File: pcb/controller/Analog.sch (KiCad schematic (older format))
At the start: 0 parts

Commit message: controller schematic capture almost done
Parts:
- added C? (x16): 0.47u, symbol Device:C
- added C? (x5): C, symbol Device:C
- added C? (x6): 4.7u, symbol Device:C
- added D? (x2): D, symbol Device:D
- added FB? (x2): Ferrite_Bead, symbol Device:Ferrite_Bead
- added J? (x2): Conn_Coaxial, symbol Connector:Conn_Coaxial
- added R? (x17): R, symbol Device:R
- added R?: 51, symbol Device:R
- added U?: TLV3501AIDBVR, symbol wbraun_ic_lib:TLV3501AIDBVR
- added U?: MCP6561-OT, Package_TO_SOT_SMD:SOT-23-5, symbol Amplifier_Operational:MCP6561-OT
- added U?: AD9609, symbol wbraun_ic_lib:AD9609
- added U?: THS4551RGT, symbol wbraun_ic_lib:THS4551RGT
- added U?: SG3225, symbol wbraun_ic_lib:SG3225
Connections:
- new net: C?.1, R?.1, R?.2, U?.1 (-)
- new net: C?.2, R?.2, U?.3 (+)
- new net: R?.1, R?.2, R?.2, U?.3 (+)
- new net: R?.1, R?.2, U?.4 (-)
- new net: C?.2, U?.1 (CLK+)
- new net: C?.2, U?.2 (CLK-)
- new net: C?.2, D?.1 (K), D?.2 (A), J?.1 (In)
- new net: C?.2, J?.1 (In), R?.2
- new net: C?.1, R?.1, U?.1 (FB-)
- new net: C?.2, R?.1, U?.2 (IN+)
- new net: C?.2, R?.1, U?.3 (IN-)
- new net: C?.1, R?.1, U?.4 (FB+)
- new net: C?.1, R?.1, R?.2, R?.2
- new net: C?.1, R?.2 (x3)
- new net: C?.2, R?.1, R?.2, R?.2
- new net +1V8: C?.2, C?.2, C?.2, C?.2, C?.2, U?.24 (AVDD), U?.29 (AVDD), U?.3 (AVDD), U?.32 (AVDD)
- new net +24V: R?.1
- new net +3V3: C?.1, C?.2, C?.2, C?.2, C?.2, FB?.2, FB?.2, R?.1, R?.2, U?.12 (~PD), U?.4 (+), U?.5 (V+), U?.5 (VS+), U?.6 (VS+), U?.7 (VS+), U?.8 (VS+)
- new net ADC_CSB: U?.4 (CSB)
- new net ADC_D0: U?.11 (D0)
- new net ADC_D1: U?.12 (D1)
- new net ADC_D2: U?.14 (D2)
- new net ADC_D3: U?.15 (D3)
- new net ADC_D4: U?.16 (D4)
- new net ADC_D5: U?.17 (D5)
- new net ADC_D6: U?.18 (D6)
- new net ADC_D7: U?.19 (D7)
- new net ADC_D8: U?.20 (D8)
- new net ADC_D9: U?.21 (D9)
- new net ADC_DCO: U?.22 (DCO)
- new net ADC_MODE: U?.23 (MODE/OR)
- new net ADC_N: U?.11 (OUT-), U?.30 (VIN-)
- new net ADC_P: U?.10 (OUT+), U?.31 (VIN+)
- new net ADC_SCLK: U?.5 (SCLK/DFS)
- new net ADC_SDIO: U?.6 (SDIO/PWDN)
- new net CLK_DVDD: C?.2, C?.2, FB?.1, U?.1 (OE), U?.6 (VCC)
- new net CLK_N: C?.1, R?.2, U?.5 (~OUT)
- new net CLK_P: C?.1, R?.1, U?.4 (OUT)
- new net DVDD: C?.2, C?.2, FB?.1, U?.13 (DVDD)
- new net GND: C?.1, C?.1, C?.1, C?.1, C?.1, C?.1, C?.1, C?.1, C?.1, C?.1, C?.1, C?.1, C?.1, C?.1, C?.1, C?.1, C?.1, C?.2, C?.2, D?.1 (K), D?.2 (A), J?.2 (Ext), J?.2 (Ext), R?.1, R?.1, R?.1, R?.2, R?.2, U?.13 (VS-), U?.14 (VS-), U?.15 (VS-), U?.16 (VS-), U?.17 (EP), U?.2 (-), U?.2 (V-), U?.26 (SENSE), U?.3 (GND), U?.33 (GND), U?.6 (PWDN)
- new net RBIAS: R?.2, U?.28 (RBIAS)
- new net UVLO: R?.1, U?.1
- new net VCM: C?.2, C?.2, U?.27 (VCM), U?.9 (VOCM)
- new net VREF: C?.2, C?.2, U?.25 (VREF)
- new net ZCS_DETECT: R?.1, R?.1, U?.5
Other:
- note added: "24V rail UVLO"
- note added: "Second Order Filter"

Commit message: started assigning footprints
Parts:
- gave numbers to parts that had none: 56

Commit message: pcb component placement almost done
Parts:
- removed C7021: 4.7u, symbol Device:C
- removed C7023, C7027: 0.47u, symbol Device:C
- removed FB7002: Ferrite_Bead, symbol Device:Ferrite_Bead
- added C7028: C, Capacitor_SMD:C_0402_1005Metric, symbol Device:C
- added C7029: 4.7u, Capacitor_SMD:C_0402_1005Metric, symbol Device:C
- added C7030: 0.47u, Capacitor_SMD:C_0402_1005Metric, symbol Device:C
- added R7019, R7020, R7021, R7022: R, Resistor_SMD:R_0402_1005Metric, symbol Device:R
- C7001, C7002, C7003, C7004, C7005, C7006, C7007, C7008, C7009, C7010, C7011, C7012, C7013, C7014, C7015, C7016, C7017, C7018, C7019, C7020, C7022, C7024, C7025, C7026: footprint (none) -> Capacitor_SMD:C_0402_1005Metric
- D7001, D7002: footprint (none) -> Diode_SMD:D_SOD-123
- FB7001: footprint (none) -> Inductor_SMD:L_0805_2012Metric
- J7001, J7002: footprint (none) -> Connector_Coaxial:SMA_Amphenol_132134-16_Vertical
- R7001: footprint (none) -> Resistor_SMD:R_2512_6332Metric
- R7002, R7003, R7004, R7005, R7006, R7007, R7008, R7009, R7010, R7011, R7012, R7013, R7014, R7015, R7016, R7017, R7018: footprint (none) -> Resistor_SMD:R_0402_1005Metric
- U7002: footprint (none) -> Package_TO_SOT_SMD:SOT-23-6
- U7003: footprint (none) -> Package_DFN_QFN:QFN-16-1EP_3x3mm_P0.5mm_EP1.8x1.8mm
- U7004: footprint (none) -> wbraun_smd:SG3225
- U7005: footprint (none) -> Package_DFN_QFN:QFN-32-1EP_5x5mm_P0.5mm_EP3.45x3.45mm
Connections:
- net +3V3: now also R7022.2
- net ADC_N: now also C7028.2, R7019.1; no longer U7003.11 (OUT-)
- net ADC_P: now also C7028.1, R7020.1; no longer U7003.10 (OUT+)
- net GND: now also C7029.1, C7030.1, R7021.1
- net at C7006.2, R7013.2, U7002.3 (+): now also R7021.2, R7022.1
- net DVDD renamed +3V3D
- net +3V3D: now also C7029.2, C7030.2
- new net: R7020.2, U7003.10 (OUT+)
- new net: R7019.2, U7003.11 (OUT-)
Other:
- moved on the sheet: C7001, C7006, C7009, C7010, C7011, C7013, C7015, D7001, D7002, J7001, R7007, R7008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

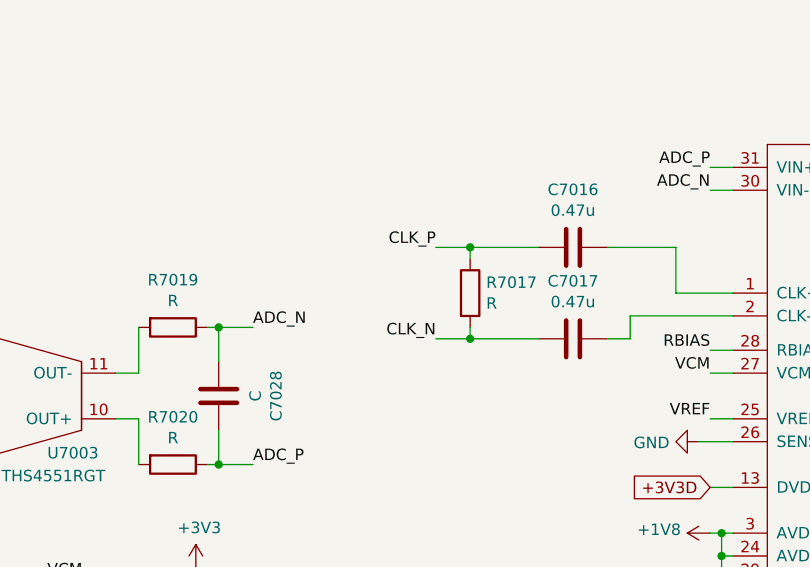
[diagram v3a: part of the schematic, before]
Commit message: controller PCB routing progress
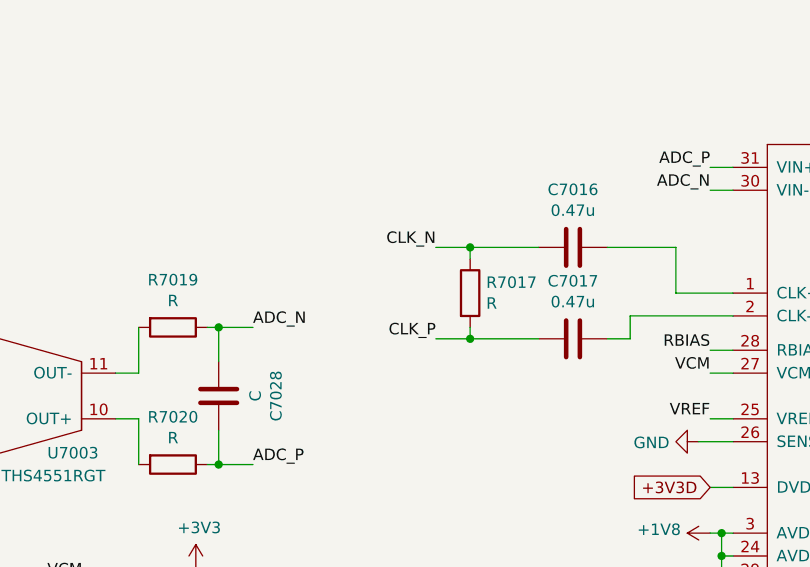
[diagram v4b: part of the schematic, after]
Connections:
- net CLK_N: now also C7016.1, R7017.1; no longer C7017.1, R7017.2
- net CLK_P: now also C7017.1, R7017.2; no longer C7016.1, R7017.1
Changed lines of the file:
@@
 Connection ~ 7100 3600
 Connection ~ 7100 4000
+Text Label 6950 4000 2    50   ~ 0
+CLK_P
 Text Label 6950 3600 2    50   ~ 0
-CLK_P
-Text Label 6950 4000 2    50   ~ 0
 CLK_N
 Text GLabel 4350 2150 2    50   Input ~ 0
